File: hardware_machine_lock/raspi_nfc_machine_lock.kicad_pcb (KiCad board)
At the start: 2 copper layers, 160 x 100 mm, 132 parts, among them J101 Raspberry_Pi_2_3, J102 Conn_01x04, J105 Conn_01x08, J106 Screw_Terminal_01x03, J107 Screw_Terminal_01x02, J108 Screw_Terminal_01x02, K101 G5Q-1A, Q101 MMBT3904, Q103 MMBT3904, U101 74HC14, U102 LM2596S-5.0, U103 MIC5205-3.3YM5, U104 PN532, U105 ADS1115IDGS, U106 LM393, U107 TL431DBZ, Y101 27.12 MHz

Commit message: Update KiCad version
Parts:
- removed C108, C109, C114, C115, C116, C117, C120, C122, C123: 100n, Capacitors_SMD:C_0603
- removed C111, C121: 10u, Capacitors_SMD:C_0603
- removed C112, C113, C124, C127: 22p, Capacitors_SMD:C_0603
- removed C118, C119: 1n, Capacitors_SMD:C_0603
- removed C125, C126: 220p, Capacitors_SMD:C_0603
- removed C128, C129, C132, C133: NC, Capacitors_SMD:C_0603
- removed C130, C131: 100p, Capacitors_SMD:C_0603
- removed FB101, FB102: Ferrite_Bead, Inductor_SMD:L_0603_1608Metric
- removed L102: 560n, Resistors_SMD:R_0805
- removed R131: 2k2, Resistors_SMD:R_0603
- removed R136: 10k, Resistors_SMD:R_0603
- removed R137, R138: 1k6, Resistors_SMD:R_0603
- removed R139, R140: 1R5, Resistors_SMD:R_0603
- removed R141, R142: NC, Resistors_SMD:R_0603
- removed RV101, RV102: 20k, Potentiometer_SMD:Potentiometer_Bourns_3214J_Horizontal
- removed TP101, TP102: TestPoint, Measurement_Points:Test_Point
- removed U103: MIC5205-3.3YM5, Package_TO_SOT_SMD:SOT-23-5
- removed U104: PN532, Housings_DFN_QFN:QFN-40-1EP_6x6mm_Pitch0.5mm
- removed U106: LM393, Housings_SOIC:SO-8_5.3x6.2mm_Pitch1.27mm
- removed U107: TL431DBZ, Package_TO_SOT_SMD:SOT-23
- removed Y101: 27.12 MHz, Crystals:Crystal_SMD_3225-4pin_3.2x2.5mm
- moved J101 198.0 mm to (202.0, 61.0)
- moved Q103 163.6 mm to (191.5, 125.0)
- moved R129 163.6 mm to (188.7, 122.2)
- moved R130 163.6 mm to (198.0, 127.0)
- moved D112 154.6 mm to (134.0, 143.0), turned to 180 degrees
- moved C134 146.1 mm to (134.0, 137.5), turned to 0 degrees
- moved D111 144.8 mm to (142.5, 143.0), turned to 180 degrees
- moved D110 136.4 mm to (151.0, 143.0), turned to 180 degrees
- moved R124 135.4 mm to (150.8, 113.0), turned to 0 degrees
- moved R125 132.6 mm to (150.2, 115.5)
- moved R134 132.6 mm to (150.2, 118.5)
- moved R135 132.6 mm to (150.2, 122.5)
- moved D109 129.4 mm to (160.0, 143.0), turned to 180 degrees
- moved R132 125.4 mm to (176.5, 144.5), turned to 180 degrees
- moved D108 124.3 mm to (169.5, 143.0), turned to 180 degrees
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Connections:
- L103 pad 1: Net-(C126-Pad1) -> (no net)
- L103 pad 2: Net-(L103-Pad2) -> (no net)
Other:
- net class Default removed
- net class Power removed

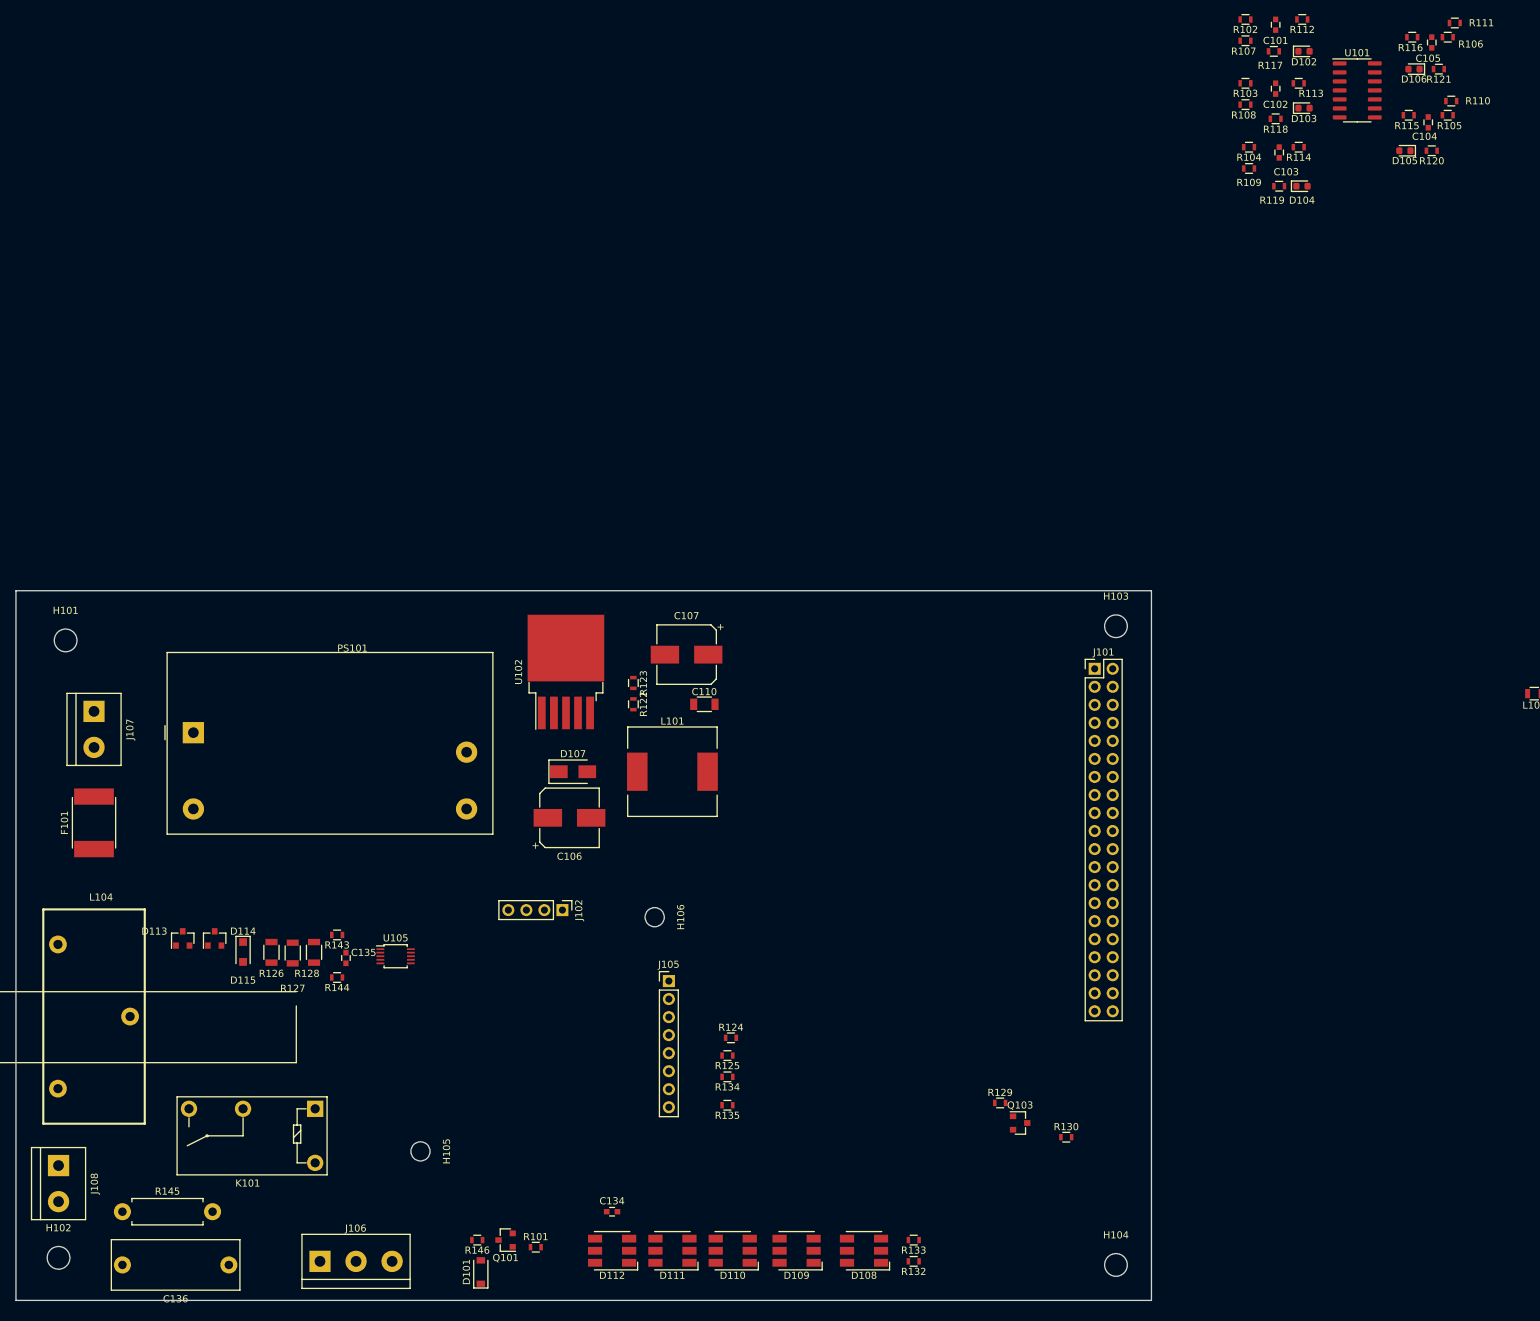
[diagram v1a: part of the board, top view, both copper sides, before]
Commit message: WIP commit to share. PSK10D, relay and current transformer confirmed with a print
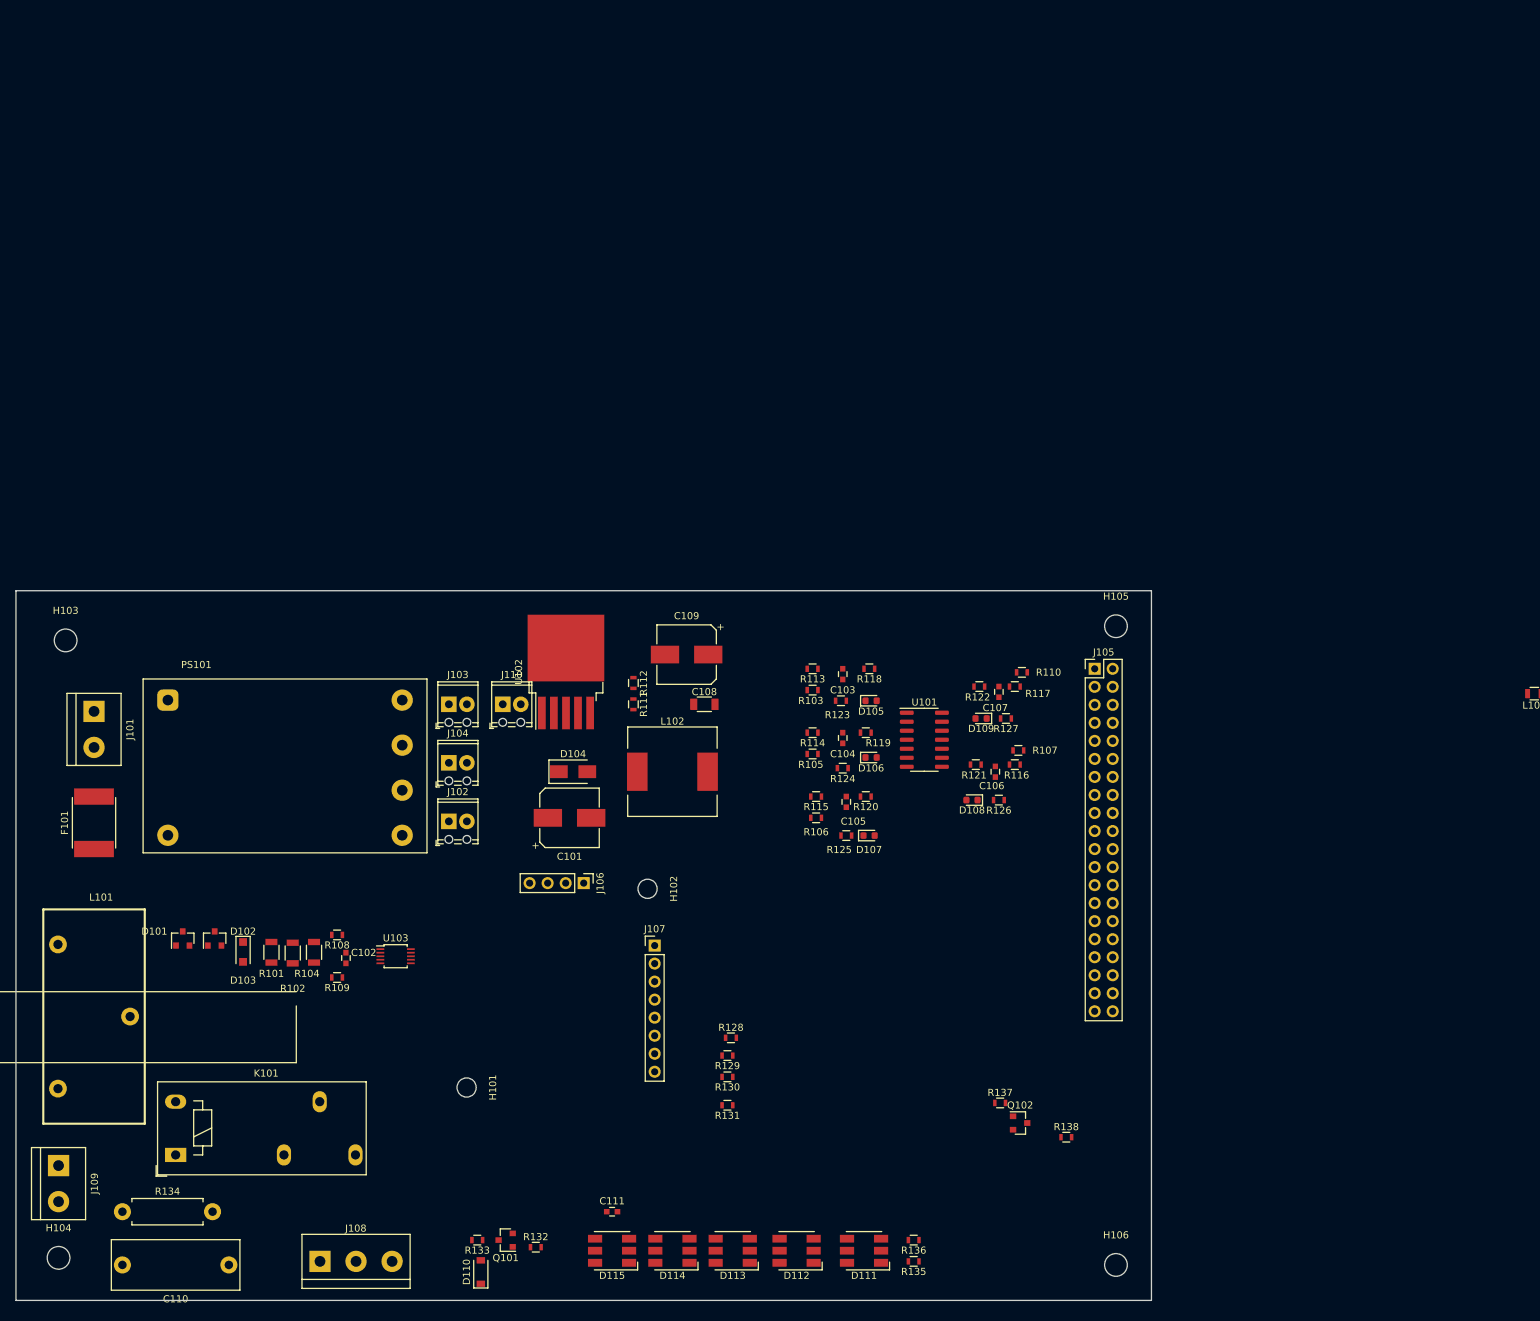
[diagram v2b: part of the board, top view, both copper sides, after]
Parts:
- added J102: Screw_Terminal_01x02, TerminalBlock_Phoenix:TerminalBlock_Phoenix_MPT-0,5-2-2.54_1x02_P2.54mm_Horizontal, F.Cu at (111.0, 82.5)
- added J103: Screw_Terminal_01x02, TerminalBlock_Phoenix:TerminalBlock_Phoenix_MPT-0,5-2-2.54_1x02_P2.54mm_Horizontal, F.Cu at (111.0, 66.0)
- added J104: Screw_Terminal_01x02, TerminalBlock_Phoenix:TerminalBlock_Phoenix_MPT-0,5-2-2.54_1x02_P2.54mm_Horizontal, F.Cu at (111.0, 74.2)
- added J110: BUZZER, TerminalBlock_Phoenix:TerminalBlock_Phoenix_MPT-0,5-2-2.54_1x02_P2.54mm_Horizontal, F.Cu at (118.6, 66.0)
- K101: value G5Q-1A -> RT314A24; footprint Relay_THT:Relay_SPST_Omron-G5Q-1A -> Relay_THT:Relay_SPDT_Schrack-RT1-FormC_RM5mm
- L101: renamed from L104; value AC1030 -> CST-1030
- PS101: value IRM-10-12 -> PSK-10D-12; footprint Converter_ACDC:Converter_ACDC_MeanWell_IRM-10-xx_THT -> nfc_lock:CUI_PSK-10-D
- R101: renamed from R126; value 200 -> 301
- R102: renamed from R127; value 200 -> 301
- R104: renamed from R128; value 200 -> 301
- moved C103 110.0 mm to (166.5, 61.8)
- moved C104 110.0 mm to (166.5, 70.8)
- moved C105 110.0 mm to (167.0, 79.8)
- moved C106 110.0 mm to (188.0, 75.5)
- moved C107 110.0 mm to (188.5, 64.2)
- moved D105 110.0 mm to (170.5, 65.5)
- moved D106 110.0 mm to (170.5, 73.5)
- moved D107 110.0 mm to (170.2, 84.5)
- moved D108 110.0 mm to (184.7, 79.5)
- moved D109 110.0 mm to (186.0, 68.0)
- moved R103 110.0 mm to (162.2, 64.0)
- moved R105 110.0 mm to (162.2, 73.0)
- moved R106 110.0 mm to (162.8, 82.0)
- moved R107 110.0 mm to (191.2, 72.5)
- moved R110 110.0 mm to (191.8, 61.5)
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- renumbered C106 to C101, C135 to C102, C101 to C103, C102 to C104, C103 to C105, C104 to C106, C105 to C107, C110 to C108, C107 to C109, C136 to C110, C134 to C111, D113 to D101, D114 to D102, D115 to D103, D107 to D104, D102 to D105, D103 to D106, D104 to D107, D105 to D108, D106 to D109, D101 to D110, D108 to D111, D109 to D112, D110 to D113, D111 to D114, D112 to D115, H105 to H101, H106 to H102, H101 to H103, H102 to H104, H103 to H105, H104 to H106, J107 to J101, J101 to J105, J102 to J106, J105 to J107, J106 to J108, J108 to J109, L101 to L102, Q103 to Q102, R107 to R103, R108 to R105, R109 to R106, R110 to R107, R143 to R108, R144 to R109, R111 to R110, R122 to R111, R123 to R112, R102 to R113, R103 to R114, R104 to R115, R105 to R116, R106 to R117, R112 to R118, R113 to R119, R114 to R120, R115 to R121, R116 to R122, R117 to R123, R118 to R124, R119 to R125, R120 to R126, R121 to R127, R124 to R128, R125 to R129, R134 to R130, R135 to R131, R101 to R132, R146 to R133, R145 to R134, R132 to R135, R133 to R136, R129 to R137, R130 to R138, U105 to U103
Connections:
- C110 pad 2: Net-(C136-Pad2) -> Net-(C110-Pad2)
- D110 pad 2: Net-(D101-Pad2) (its old number) -> Net-(D110-Pad2)
- D115 pad 5: (no net) -> unconnected-(D115-Pad5)
- D115 pad 6: (no net) -> unconnected-(D115-Pad6)
- J101 pad 1: Net-(J107-Pad1) -> Net-(J101-Pad1)
- J105 pad 10: (no net) -> unconnected-(J105-Pad10)
- J105 pad 13: (no net) -> unconnected-(J105-Pad13)
- J105 pad 18: (no net) -> unconnected-(J105-Pad18)
- J105 pad 22: (no net) -> unconnected-(J105-Pad22)
- J105 pad 26: (no net) -> unconnected-(J105-Pad26)
- J105 pad 27: (no net) -> unconnected-(J105-Pad27)
- J105 pad 28: (no net) -> unconnected-(J105-Pad28)
- J105 pad 29: (no net) -> unconnected-(J105-Pad29)
- J105 pad 31: (no net) -> unconnected-(J105-Pad31)
- J105 pad 33: (no net) -> unconnected-(J105-Pad33)
- J105 pad 35: (no net) -> unconnected-(J105-Pad35)
- J105 pad 36: (no net) -> unconnected-(J105-Pad36)
- J105 pad 37: (no net) -> unconnected-(J105-Pad37)
- J105 pad 8: (no net) -> unconnected-(J105-Pad8)
- J106 pad 1: (no net) -> unconnected-(J106-Pad1)
- J106 pad 2: (no net) -> unconnected-(J106-Pad2)
- J106 pad 3: (no net) -> unconnected-(J106-Pad3)
- J106 pad 4: (no net) -> unconnected-(J106-Pad4)
- J107 pad 1: (no net) -> unconnected-(J107-Pad1)
- J107 pad 2: (no net) -> unconnected-(J107-Pad2)
- J108 pad 1: Net-(D101-Pad2) (its old number) -> Net-(D110-Pad2)
- J109 pad 1: Net-(J108-Pad1) -> Net-(J109-Pad1)
- J109 pad 2: Net-(C136-Pad2) -> Net-(C110-Pad2)
- PS101 pad 1: Net-(J107-Pad1) -> Net-(F101-Pad1)
- PS101 pad 2: Net-(F101-Pad1) -> Net-(J101-Pad1)
- PS101 pad 3: GND -> (no net)
- Q102 pad 3: (no net) -> /BUZZ
- R133 pad 2: Net-(D101-Pad2) (its old number) -> Net-(D110-Pad2)
- R134 pad 1: Net-(J108-Pad1) -> Net-(J109-Pad1)
- R138 pad 2: (no net) -> Net-(J110-Pad1)
- U101 pad 12: (no net) -> unconnected-(U101-Pad12)
- U103 pad 2: (no net) -> unconnected-(U103-Pad2)
- U103 pad 5: (no net) -> unconnected-(U103-Pad5)
- U103 pad 6: (no net) -> unconnected-(U103-Pad6)
- U103 pad 7: (no net) -> unconnected-(U103-Pad7)
